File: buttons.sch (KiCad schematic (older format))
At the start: 4 parts, among them SW1 UP, SW2 DOWN

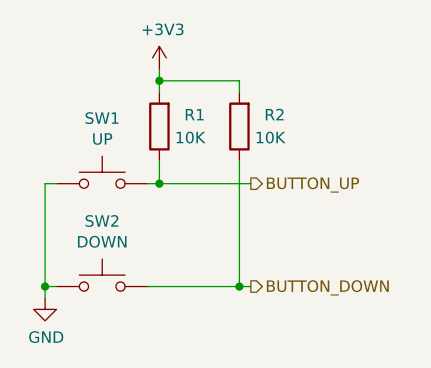
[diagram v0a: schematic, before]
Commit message: Запитал МК, добавил цепи питания, тактирования, модуль клавиатуры.
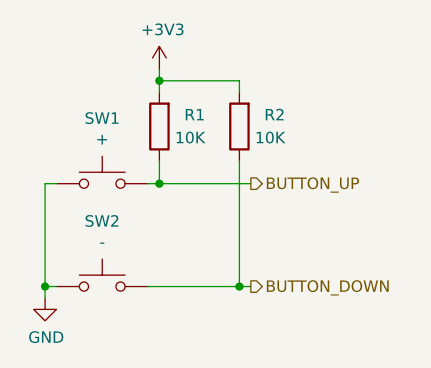
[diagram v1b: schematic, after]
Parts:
- SW1: value UP -> +
- SW2: value DOWN -> -
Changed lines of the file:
@@
 $Descr A4 11693 8268
 encoding utf-8
-Sheet 2 5
+Sheet 2 9
 Title ""
 Date "2020-04-18"
@@
 P 5250 3850
 F 0 "SW1" H 5250 4135 50  0000 C CNN
-F 1 "UP" H 5250 4044 50  0000 C CNN
+F 1 "+" H 5250 4044 50  0000 C CNN
 F 2 "Button_Switch_THT:SW_Tactile_SPST_Angled_PTS645Vx83-2LFS" H 5250 4050 50  0001 C CNN
 F 3 "~" H 5250 4050 50  0001 C CNN
@@
 P 5250 4300
 F 0 "SW2" H 5250 4585 50  0000 C CNN
-F 1 "DOWN" H 5250 4494 50  0000 C CNN
+F 1 "-" H 5250 4494 50  0000 C CNN
 F 2 "Button_Switch_THT:SW_Tactile_SPST_Angled_PTS645Vx83-2LFS" H 5250 4500 50  0001 C CNN
 F 3 "~" H 5250 4500 50  0001 C CNN
@@
 $EndComp
 $Comp
-L power:GND #PWR05
+L power:GND #PWR06
 U 1 1 5EB94F12
 P 5000 4350
-F 0 "#PWR05" H 5000 4100 50  0001 C CNN
+F 0 "#PWR06" H 5000 4100 50  0001 C CNN
 F 1 "GND" H 5005 4177 50  0000 C CNN
 F 2 "" H 5000 4350 50  0001 C CNN
@@
 BUTTON_DOWN
 $Comp
-L power:+3V3 #PWR06
+L power:+3V3 #PWR07
 U 1 1 5EC7718C
 P 5500 3350
-F 0 "#PWR06" H 5500 3200 50  0001 C CNN
+F 0 "#PWR07" H 5500 3200 50  0001 C CNN
 F 1 "+3V3" H 5515 3523 50  0000 C CNN
 F 2 "" H 5500 3350 50  0001 C CNN

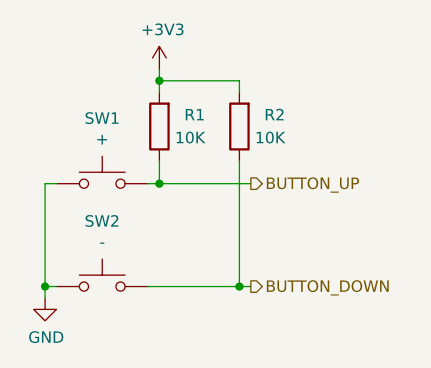
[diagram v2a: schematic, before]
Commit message: dcdc доделан на 5V.
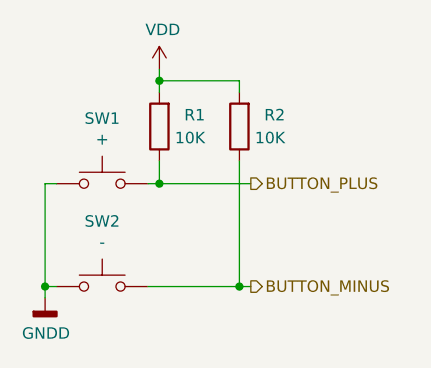
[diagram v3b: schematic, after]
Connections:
- net +3V3 renamed VDD
- net BUTTON_DOWN renamed BUTTON_MINUS
- net BUTTON_UP renamed BUTTON_PLUS
- net GND renamed GNDD
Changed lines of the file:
@@
-	1    0    0    -1
-$EndComp
-$Comp
-L power:GND #PWR06
-U 1 1 5EB94F12
-P 5000 4350
-F 0 "#PWR06" H 5000 4100 50  0001 C CNN
-F 1 "GND" H 5005 4177 50  0000 C CNN
-F 2 "" H 5000 4350 50  0001 C CNN
-F 3 "" H 5000 4350 50  0001 C CNN
-	1    5000 4350
 	1    0    0    -1
 $EndComp
@@
 $EndComp
 Text HLabel 5900 3850 2    50   Output ~ 0
-BUTTON_UP
+BUTTON_PLUS
 Text HLabel 5900 4300 2    50   Output ~ 0
-BUTTON_DOWN
+BUTTON_MINUS
+Wire Wire Line
+	5850 3400 5500 3400
+Connection ~ 5500 3400
+Wire Wire Line
+	5500 3400 5500 3450
 $Comp
-L power:+3V3 #PWR07
-U 1 1 5EC7718C
+L power:VDD #PWR041
+U 1 1 5EA4E537
 P 5500 3350
-F 0 "#PWR07" H 5500 3200 50  0001 C CNN
-F 1 "+3V3" H 5515 3523 50  0000 C CNN
+F 0 "#PWR041" H 5500 3200 50  0001 C CNN
+F 1 "VDD" H 5515 3523 50  0000 C CNN
 F 2 "" H 5500 3350 50  0001 C CNN
 F 3 "" H 5500 3350 50  0001 C CNN
@@
 	1    0    0    -1
 $EndComp
-Wire Wire Line
-	5850 3400 5500 3400
-Connection ~ 5500 3400
-Wire Wire Line
-	5500 3400 5500 3450
+$Comp
+L power:GNDD #PWR07
+U 1 1 5EA4EB44
+P 5000 4350
+F 0 "#PWR07" H 5000 4100 50  0001 C CNN
+F 1 "GNDD" H 5004 4195 50  0000 C CNN
+F 2 "" H 5000 4350 50  0001 C CNN
+F 3 "" H 5000 4350 50  0001 C CNN
+	1    5000 4350
+	1    0    0    -1
+$EndComp
 $EndSCHEMATC

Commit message: Расставил проверенные блоки в столбец.
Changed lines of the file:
@@
 U 1 1 5EB94F23
 P 5850 3600
-F 0 "R2" H 5650 3550 50  0000 L CNN
+F 0 "R2" H 5700 3550 50  0000 L CNN
 F 1 "10K" H 5650 3650 50  0000 L CNN
 F 2 "Resistor_SMD:R_0603_1608Metric_Pad1.05x0.95mm_HandSolder" V 5780 3600 50  0001 C CNN
@@
 U 1 1 5EB94F1D
 P 5500 3600
-F 0 "R1" H 5300 3550 50  0000 L CNN
+F 0 "R1" H 5350 3550 50  0000 L CNN
 F 1 "10K" H 5300 3650 50  0000 L CNN
 F 2 "Resistor_SMD:R_0603_1608Metric_Pad1.05x0.95mm_HandSolder" V 5430 3600 50  0001 C CNN
